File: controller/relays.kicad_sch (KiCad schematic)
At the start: 32 parts, among them K1 G2RK-1-DC5, K2 G2RK-1-DC5, K3 G2RK-1-DC5, K4 G2RK-1-DC5, K5 G2RK-1-DC5, K6 G2RK-1-DC5, K7 G2RK-1-DC5, K8 G2RK-1-DC5, Q1 BS170, Q10 BS170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

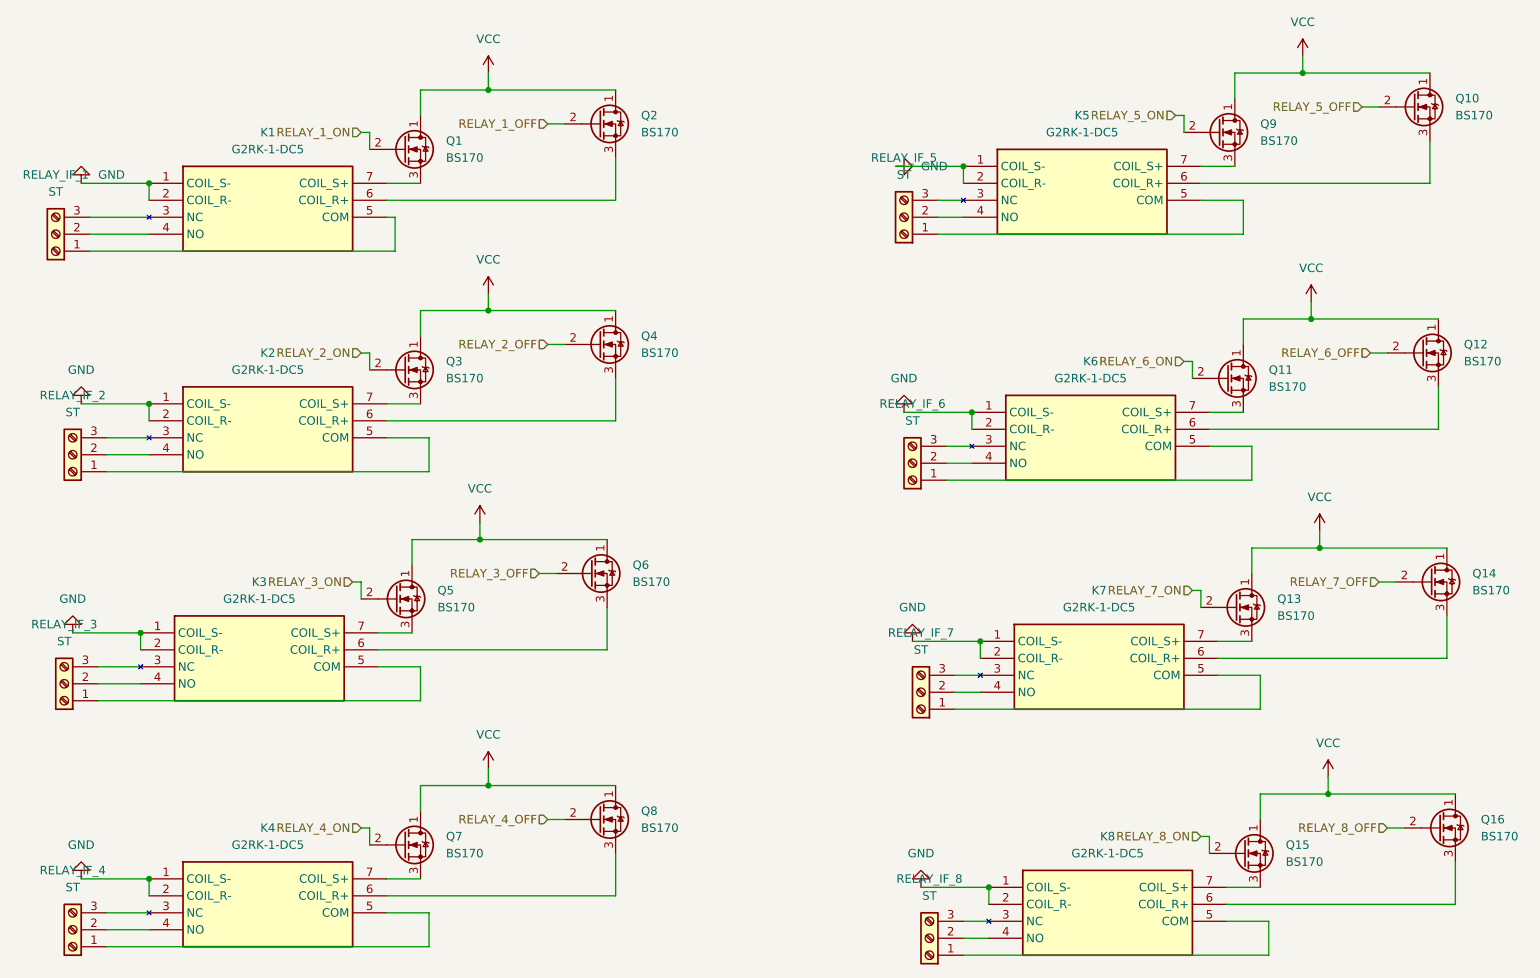
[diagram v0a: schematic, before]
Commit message: made symbols and footprint relative to project
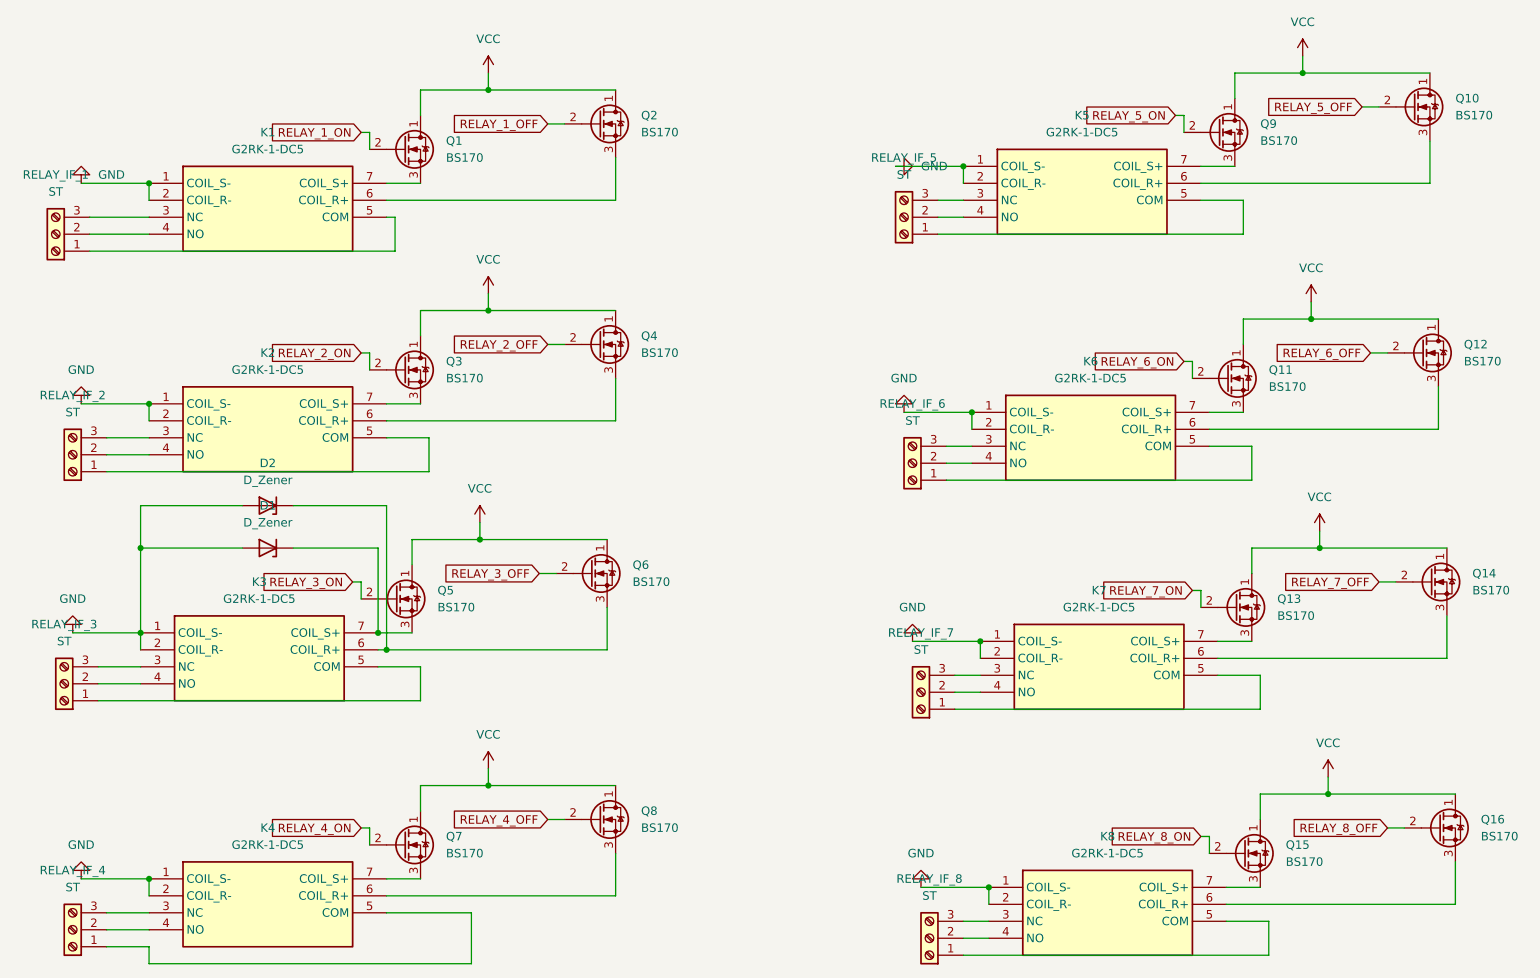
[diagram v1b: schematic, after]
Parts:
- added D1, D2: D_Zener, symbol Device:D_Zener
- K1, K2, K3, K4, K5, K6, K7, K8: footprint G2RK1DC5 -> arduino-library:G2RK1DC5
- RELAY_IF_1, RELAY_IF_2, RELAY_IF_3, RELAY_IF_4, RELAY_IF_5, RELAY_IF_6, RELAY_IF_7, RELAY_IF_8: footprint (none) -> arduino-library:TBL00138103GY2GY
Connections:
- net GND: now also D1.2 (A), D2.2 (A)
- net at K3.6 (COIL_R+), Q6.3 (S): now also D2.1 (K)
- net at K3.7 (COIL_S+), Q5.3 (S): now also D1.1 (K)
